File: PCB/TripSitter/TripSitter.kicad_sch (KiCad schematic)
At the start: 0 parts

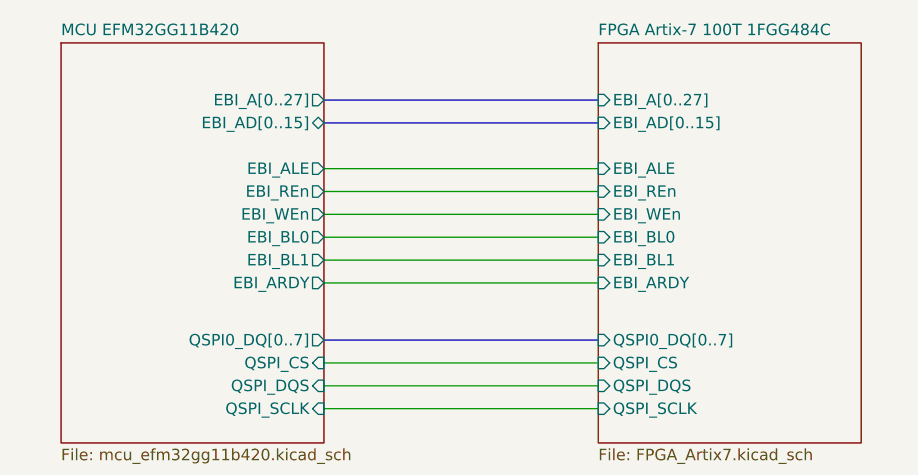
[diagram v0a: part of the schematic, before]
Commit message: pcb: re-structured PCB schematic layout (#17)
Co-authored-by: Sigvart Hovland <sigvart.m@gmail.com>
Co-authored-by: Ida-Sofie Pettersen <idasofie@Ida-Sofies-MacBook-Air.local>
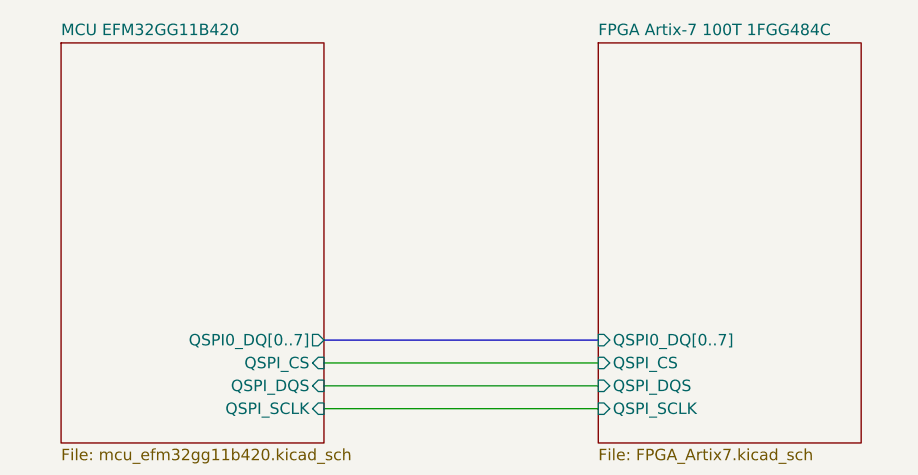
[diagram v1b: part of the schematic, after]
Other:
- sheet FPGA Artix-7 100T 1FGG484C ports: added none; removed EBI_AD[0..15], EBI_ALE, EBI_ARDY, EBI_A[0..27], EBI_BL0, EBI_BL1, EBI_REn, EBI_WEn
- sheet MCU EFM32GG11B420 ports: added none; removed EBI_AD[0..15], EBI_ALE, EBI_ARDY, EBI_A[0..27], EBI_BL0, EBI_BL1, EBI_REn, EBI_WEn
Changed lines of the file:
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@@
-    (stroke (width 0) (type default))
-  )
-  (wire (pts (xy 119.38 48.26) (xy 149.86 48.26))
-    (stroke (width 0) (type default))
-  )
-  (wire (pts (xy 119.38 43.18) (xy 149.86 43.18))
-    (stroke (width 0) (type default))
-  )
-  (wire (pts (xy 119.38 45.72) (xy 149.86 45.72))
-    (stroke (width 0) (type default))
-  )
-  (bus (pts (xy 119.38 27.94) (xy 149.86 27.94))
-    (stroke (width 0) (type default))
-  )
-  (wire (pts (xy 119.38 35.56) (xy 149.86 35.56))
     (stroke (width 0) (type default))
   )
@@
     (stroke (width 0) (type default))
   )
-  (wire (pts (xy 119.38 38.1) (xy 149.86 38.1))
-    (stroke (width 0) (type default))
-  )
-  (wire (pts (xy 119.38 40.64) (xy 149.86 40.64))
-    (stroke (width 0) (type default))
-  )
   (bus (pts (xy 119.38 54.61) (xy 149.86 54.61))
-    (stroke (width 0) (type default))
-  )
-  (bus (pts (xy 119.38 30.48) (xy 149.86 30.48))
     (stroke (width 0) (type default))
   )
@@
     (property "Sheetfile" "FPGA_Artix7.kicad_sch" (at 149.86 66.6246 0)
       (effects (font (size 1.27 1.27)) (justify left top))
-    )
-    (pin "EBI_A[0..27]" input (at 149.86 27.94 180)
-      (effects (font (size 1.27 1.27)) (justify left))
-    )
-    (pin "EBI_AD[0..15]" input (at 149.86 30.48 180)
-      (effects (font (size 1.27 1.27)) (justify left))
-    )
-    (pin "EBI_ALE" input (at 149.86 35.56 180)
-      (effects (font (size 1.27 1.27)) (justify left))
-    )
-    (pin "EBI_REn" input (at 149.86 38.1 180)
-      (effects (font (size 1.27 1.27)) (justify left))
-    )
-    (pin "EBI_WEn" input (at 149.86 40.64 180)
-      (effects (font (size 1.27 1.27)) (justify left))
-    )
-    (pin "EBI_BL0" input (at 149.86 43.18 180)
-      (effects (font (size 1.27 1.27)) (justify left))
-    )
-    (pin "EBI_BL1" input (at 149.86 45.72 180)
-      (effects (font (size 1.27 1.27)) (justify left))
-    )
-    (pin "EBI_ARDY" input (at 149.86 48.26 180)
-      (effects (font (size 1.27 1.27)) (justify left))
     )
     (pin "QSPI_CS" input (at 149.86 57.15 180)
@@
       (effects (font (size 1.27 1.27)) (justify left top))
     )
-    (pin "EBI_A[0..27]" output (at 119.38 27.94 0)
-      (effects (font (size 1.27 1.27)) (justify right))
-    )
-    (pin "EBI_AD[0..15]" bidirectional (at 119.38 30.48 0)
-      (effects (font (size 1.27 1.27)) (justify right))
-    )
-    (pin "EBI_ALE" output (at 119.38 35.56 0)
-      (effects (font (size 1.27 1.27)) (justify right))
-    )
-    (pin "EBI_REn" output (at 119.38 38.1 0)
-      (effects (font (size 1.27 1.27)) (justify right))
-    )
-    (pin "EBI_WEn" output (at 119.38 40.64 0)
-      (effects (font (size 1.27 1.27)) (justify right))
-    )
-    (pin "EBI_BL1" output (at 119.38 45.72 0)
-      (effects (font (size 1.27 1.27)) (justify right))
-    )
-    (pin "EBI_BL0" output (at 119.38 43.18 0)
-      (effects (font (size 1.27 1.27)) (justify right))
-    )
-    (pin "EBI_ARDY" output (at 119.38 48.26 0)
-      (effects (font (size 1.27 1.27)) (justify right))
-    )
     (pin "QSPI0_DQ[0..7]" output (at 119.38 54.61 0)

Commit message: pcb: mounting holes
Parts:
- added H1, H2, H3, H4, H5, H6: MountingHole_Pad, MountingHole:MountingHole_4.3mm_M4_Pad_Via, symbol Mechanical:MountingHole_Pad
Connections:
- new net GND: H1.1, H2.1, H3.1, H4.1, H5.1, H6.1
